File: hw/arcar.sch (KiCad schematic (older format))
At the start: 55 parts, among them J1 USB_B_Micro, J2 GPIO, J3 MOTOR, M1 screw, M2 screw, M3 screw, P1 AVR_ISP_02X03, SW1 SW_Push, U1 USBLC6-2SC6, U2 ATMEGA328PB-AU, U3 CP2102, U4 ULN2003A, U5 LSM9DS1, U6 ULN2003A, U7 TLE52062GAUMA1, U8 RN4871

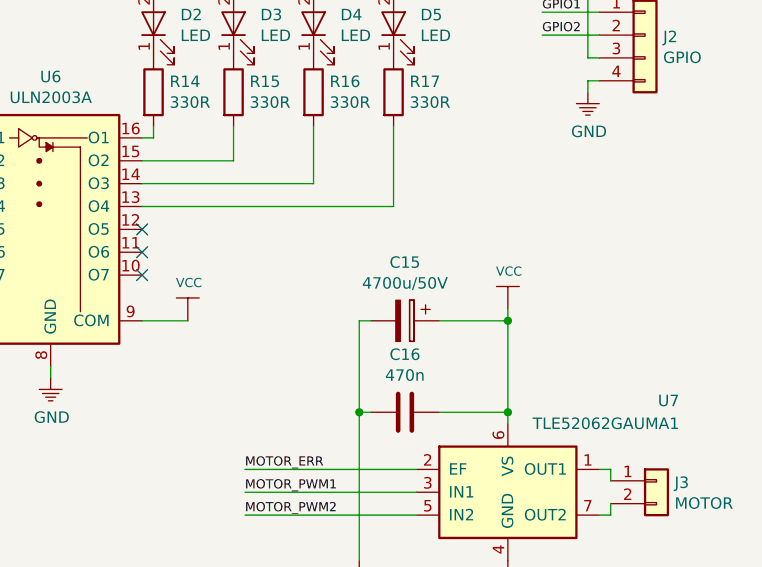
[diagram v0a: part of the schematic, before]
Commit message: assigned footprints
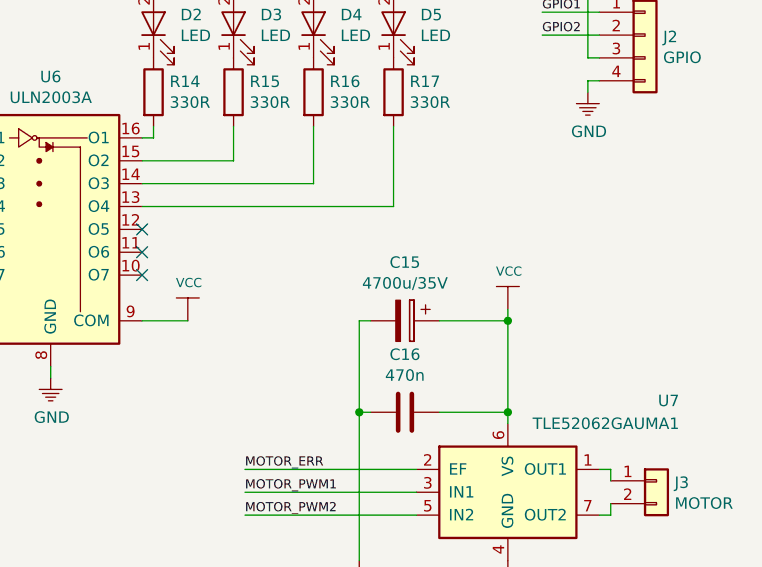
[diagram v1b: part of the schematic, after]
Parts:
- C1, C10, C11, C12, C13, C14, C16, C2, C3, C4, C5, C6, C7, C8, C9: footprint (none) -> Capacitors_SMD:C_0805_HandSoldering
- C15: value 4700u/50V -> 4700u/35V; footprint (none) -> Capacitors_THT:CP_Radial_D18.0mm_P7.50mm
- D1: footprint (none) -> Diodes_SMD:D_SMA
- D2, D3, D4, D5: footprint (none) -> LEDs:LED_D3.0mm_FlatTop
- J1: footprint Connectors:USB_Micro-B_10103594-0001LF -> Connectors_USB:USB_Micro-B_Wuerth-614105150721_Vertical_CircularHoles
- J2: footprint (none) -> Pin_Headers:Pin_Header_Straight_1x04_Pitch2.54mm
- J3: footprint (none) -> Pin_Headers:Pin_Header_Straight_1x02_Pitch2.54mm
- M1, M2, M3: footprint (none) -> wyk_mech:screw_M3
- R1, R10, R11, R12, R13, R14, R15, R16, R17, R2, R3, R4, R5, R6, R7, R8, R9: footprint (none) -> Resistors_SMD:R_0805_HandSoldering
- SW1: footprint (none) -> Buttons_Switches_THT:SW_PUSH_6mm_h5mm
- U4, U6: footprint (none) -> Housings_SOIC:SOIC-16_3.9x9.9mm_Pitch1.27mm
- U8: footprint (none) -> wyk_rf_modules:RN4871

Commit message: assigned footprints
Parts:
- AFF1: footprint Displays_7-Segment:LTS-69xx -> Displays_7-Segment:7SegmentLED_LTS6760_LTS6780
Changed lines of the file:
@@
 F 0 "AFF1" H 6750 2267 50  0000 C CNN
 F 1 "LTS-6960HR" H 6750 2176 50  0000 C CNN
-F 2 "Displays_7-Segment:LTS-69xx" H 6750 1100 50  0001 C CNN
+F 2 "Displays_7-Segment:7SegmentLED_LTS6760_LTS6780" H 6750 1100 50  0001 C CNN
 F 3 "Display/LTC-6960HR.pdf" H 6750 1600 50  0001 C CNN
 	1    6750 1600

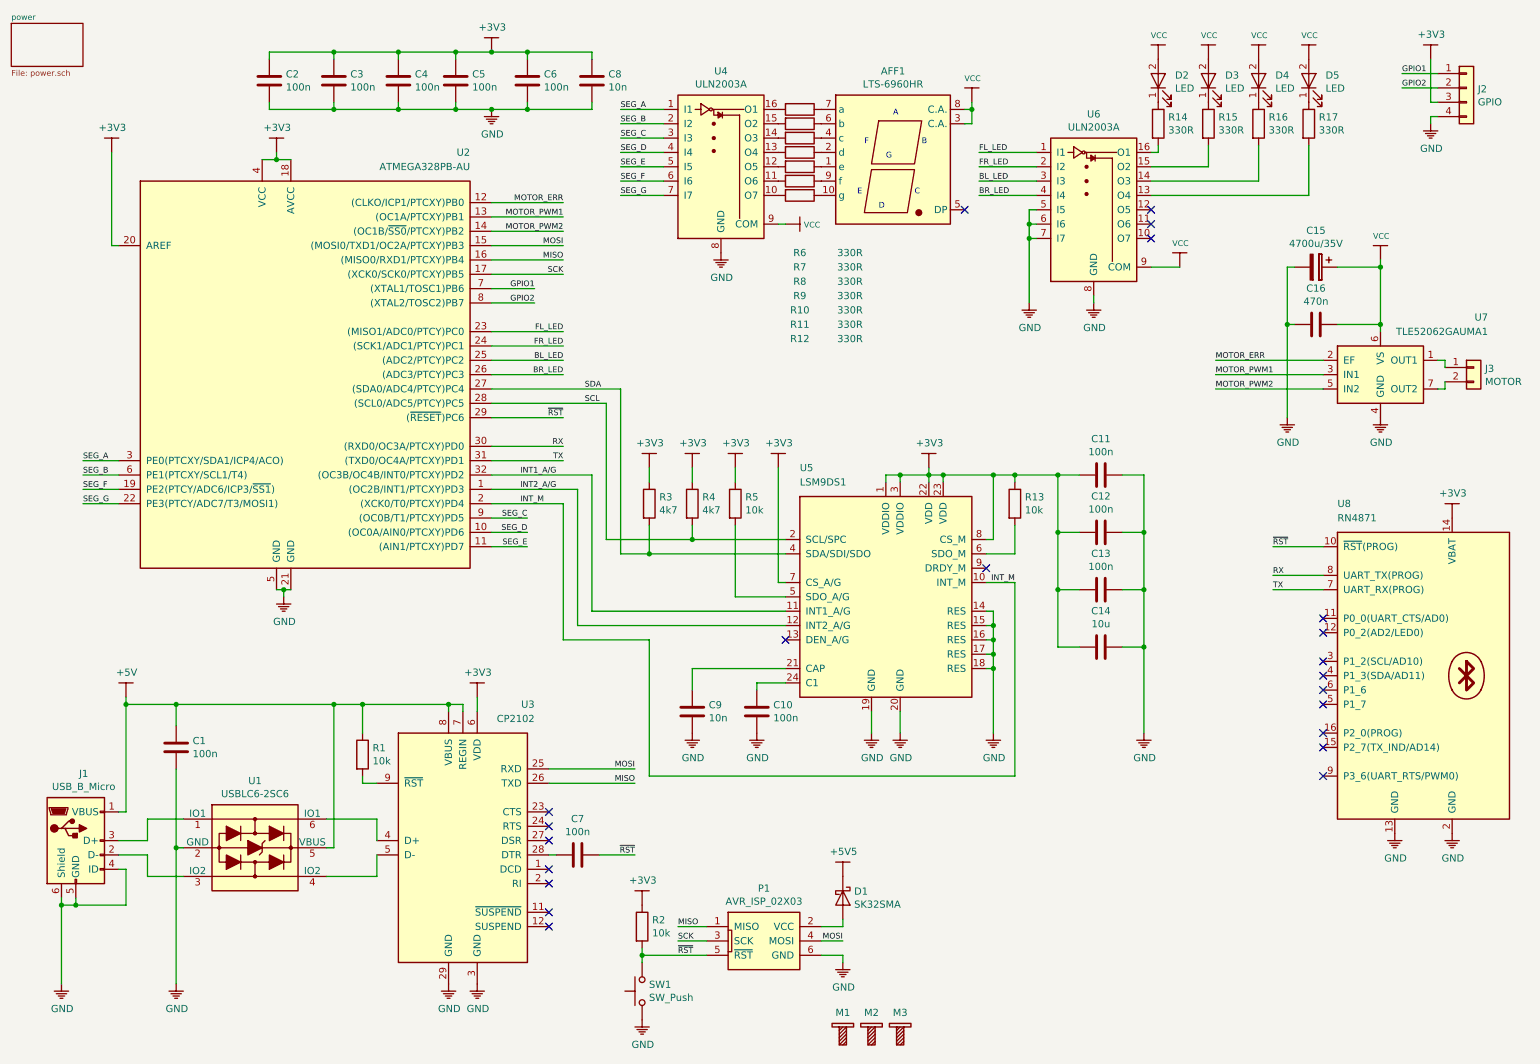
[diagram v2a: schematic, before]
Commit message: reduced schematic
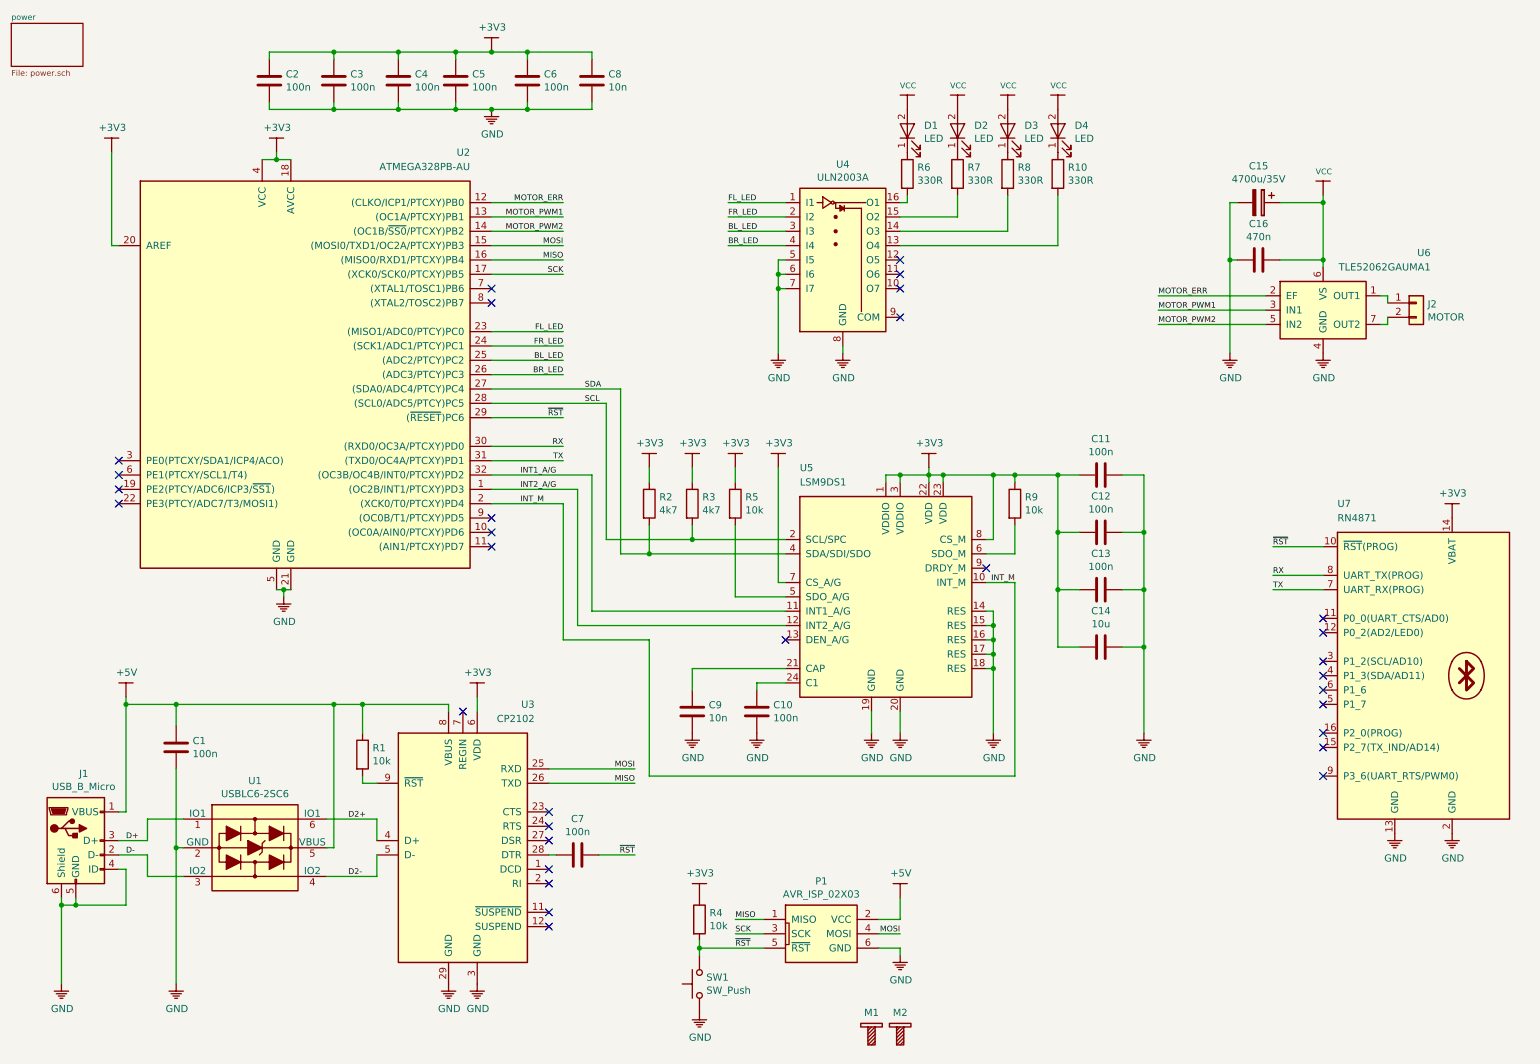
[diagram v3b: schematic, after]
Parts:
- removed AFF1: LTS-6960HR, Displays_7-Segment:7SegmentLED_LTS6760_LTS6780, symbol LTS-6960HR
- removed D1: SK32SMA, Diodes_SMD:D_SMA, symbol D_Schottky
- removed J2: GPIO, Pin_Headers:Pin_Header_Straight_1x04_Pitch2.54mm, symbol Conn_01x04
- removed M3: screw, wyk_mech:screw_M3, symbol screw
- removed R10, R11, R12, R6, R7, R8, R9: 330R, Resistors_SMD:R_0805_HandSoldering, symbol R
- removed U4: ULN2003A, Housings_SOIC:SOIC-16_3.9x9.9mm_Pitch1.27mm, symbol ULN2003A
- C15: footprint Capacitors_THT:CP_Radial_D18.0mm_P7.50mm -> Capacitors_THT:CP_Radial_D4.0mm_P1.50mm
- renumbered D2 to D1, D3 to D2, D4 to D3, D5 to D4, J3 to J2, R17 to R10, R3 to R2, R4 to R3, R2 to R4, R14 to R6, R15 to R7, R16 to R8, R13 to R9, U6 to U4, U7 to U6, U8 to U7
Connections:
- net +5V: now also P1.2 (VCC); no longer U3.7 (REGIN)
- net VCC: no longer U4.9 (COM)
- net D-: now reaches J1.2 (D-), U1.3 (IO2)
- net D+: now reaches J1.3 (D+), U1.1 (IO1)
- net D2-: now reaches U1.4 (IO2), U3.5 (D-)
- net D2+: now reaches U1.6 (IO1), U3.4 (D+)
- net GPIO1: no longer names the net of U2.7 ((XTAL1/TOSC1)PB6)
- net GPIO2: no longer names the net of U2.8 ((XTAL2/TOSC2)PB7)
- net SEG_A: no longer names the net of U2.3 (PE0(PTCXY/SDA1/ICP4/ACO))
- net SEG_B: no longer names the net of U2.6 (PE1(PTCXY/SCL1/T4))
- net SEG_C: no longer names the net of U2.9 ((OC0B/T1/PTCXY)PD5)
- net SEG_D: no longer names the net of U2.10 ((OC0A/AIN0/PTCXY)PD6)
- net SEG_E: no longer names the net of U2.11 ((AIN1/PTCXY)PD7)
- net SEG_F: no longer names the net of U2.19 (PE2(PTCY/ADC6/ICP3/~SS1~))
- net SEG_G: no longer names the net of U2.22 (PE3(PTCY/ADC7/T3/MOSI1))
- no-connect marks 22 -> 32
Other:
- note removed: "A"
- note removed: "B"
- note removed: "C"
- note removed: "D"
- note removed: "E"
- note removed: "F"
- note removed: "G"
- moved on the sheet: C15, C16, D1, D2, D3, D4, J2, M1, M2, P1, R10, R4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

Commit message: big reduced change all power source
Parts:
- added C17: 4700u/35V, Capacitors_THT:CP_Radial_D4.0mm_P1.50mm, symbol CP
- added C18, C19: 1u/50V, Capacitors_SMD:C_0805_HandSoldering, symbol C
- added D5, D6, D7, D8, D9: SK32SMA, Diodes_SMD:D_SMA, symbol D_Schottky
- added J3: POWER, Pin_Headers:Pin_Header_Straight_1x02_Pitch2.54mm, symbol Conn_01x02
- added U8: MCP1804T-3302I/DB, TO_SOT_Packages_SMD:SOT-223, symbol MCP1804T-3302I/DB
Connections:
- net +5V is gone; now on net VCC: C1.1, J1.1 (VBUS), P1.2 (VCC), R1.1, U1.5 (VBUS), U3.8 (VBUS)
- net +3V3: now also C19.1, U8.3 (VO)
- net GND: now also C17.2, C18.2, C19.2, D6.2 (A), D8.2 (A), U8.2 (GND)
- net VCC: now also D5.1 (K), D7.1 (K), D9.2 (A)
- new net: D7.2 (A), D8.1 (K), J3.1 (Pin_1)
- new net: D5.2 (A), D6.1 (K), J3.2 (Pin_2)
- new net: C17.1, C18.1, D9.1 (K), U8.1 (VI)
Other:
- moved on the sheet: C15, C16, C2, C3, C4, C5, C6, C8, D1, D2, D3, D4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

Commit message: all the components are placed on the board
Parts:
- D1, D2, D3, D4: footprint LEDs:LED_D3.0mm_FlatTop -> Pin_Headers:Pin_Header_Straight_1x02_Pitch2.54mm
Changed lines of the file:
@@
 F 0 "D1" V 5988 1083 50  0000 R CNN
 F 1 "LED" V 5897 1083 50  0000 R CNN
-F 2 "LEDs:LED_D3.0mm_FlatTop" H 5950 1200 50  0001 C CNN
+F 2 "Pin_Headers:Pin_Header_Straight_1x02_Pitch2.54mm" H 5950 1200 50  0001 C CNN
 F 3 "" H 5950 1200 50  0001 C CNN
 	1    5950 1200
@@
 F 0 "D2" V 6338 1083 50  0000 R CNN
 F 1 "LED" V 6247 1083 50  0000 R CNN
-F 2 "LEDs:LED_D3.0mm_FlatTop" H 6300 1200 50  0001 C CNN
+F 2 "Pin_Headers:Pin_Header_Straight_1x02_Pitch2.54mm" H 6300 1200 50  0001 C CNN
 F 3 "" H 6300 1200 50  0001 C CNN
 	1    6300 1200
@@
 F 0 "D3" V 6688 1083 50  0000 R CNN
 F 1 "LED" V 6597 1083 50  0000 R CNN
-F 2 "LEDs:LED_D3.0mm_FlatTop" H 6650 1200 50  0001 C CNN
+F 2 "Pin_Headers:Pin_Header_Straight_1x02_Pitch2.54mm" H 6650 1200 50  0001 C CNN
 F 3 "" H 6650 1200 50  0001 C CNN
 	1    6650 1200
@@
 F 0 "D4" V 7038 1083 50  0000 R CNN
 F 1 "LED" V 6947 1083 50  0000 R CNN
-F 2 "LEDs:LED_D3.0mm_FlatTop" H 7000 1200 50  0001 C CNN
+F 2 "Pin_Headers:Pin_Header_Straight_1x02_Pitch2.54mm" H 7000 1200 50  0001 C CNN
 F 3 "" H 7000 1200 50  0001 C CNN
 	1    7000 1200
@@
 	5950 1700 5950 1650
 Wire Wire Line
-	5400 7000 5400 7050
-Wire Wire Line
-	5400 7050 5400 7100
+	5400 7000 5400 7100
 Connection ~ 5400 7050
 Wire Wire Line
@@
 	9750 4250 9400 4250
 Wire Wire Line
-	2450 4550 2500 4550
-Wire Wire Line
-	2500 4550 2550 4550
+	2450 4550 2550 4550
 Wire Wire Line
 	2500 4600 2500 4550
 Connection ~ 2500 4550
 Wire Wire Line
-	2350 1550 2450 1550
-Wire Wire Line
-	2450 1550 2550 1550
+	2350 1550 2550 1550
 Wire Wire Line
 	2450 1500 2450 1550
@@
 	2850 6350 2850 5350
 Wire Wire Line
-	1750 5800 1750 6350
-Wire Wire Line
-	1750 6350 1750 7300
+	1750 5800 1750 7300
 Wire Wire Line
 	1750 6350 1800 6350
@@
 	1400 6100 1350 6100
 Wire Wire Line
-	1400 5300 1400 5350
-Wire Wire Line
-	1400 5350 1400 6100
+	1400 5300 1400 6100
 Wire Wire Line
 	1350 6500 1400 6500
@@
 	9700 3400 8950 3400
 Wire Wire Line
-	5050 2100 5050 2200
-Wire Wire Line
-	5050 2200 5050 2300
-Wire Wire Line
-	5050 2300 5050 2700
+	5050 2100 5050 2700
 Wire Wire Line
 	5050 2100 5100 2100
@@
 Connection ~ 5050 2300
 Wire Wire Line
-	10100 2500 10100 2550
-Wire Wire Line
-	10100 2550 10100 2950
-Wire Wire Line
-	10100 2950 10100 3000
+	10100 2500 10100 3000
 Wire Wire Line
 	9800 2950 10100 2950
@@
 Connection ~ 10100 2550
 Wire Wire Line
-	9450 2550 9450 2950
-Wire Wire Line
-	9450 2950 9450 3600
+	9450 2550 9450 3600
 Wire Wire Line
 	9450 2550 9500 2550
@@
 	7250 2700 7250 2750
 Wire Wire Line
-	6350 2700 6800 2700
-Wire Wire Line
-	6800 2700 7250 2700
-Wire Wire Line
-	7250 2700 7650 2700
-Wire Wire Line
-	7650 2700 7900 2700
-Wire Wire Line
-	7900 2700 8150 2700
-Wire Wire Line
-	8150 2700 8600 2700
+	6350 2700 8600 2700
 Wire Wire Line
 	8600 2700 8600 2750
@@
 	7250 3100 7250 3050
 Wire Wire Line
-	6350 3100 6800 3100
-Wire Wire Line
-	6800 3100 7250 3100
-Wire Wire Line
-	7250 3100 7650 3100
-Wire Wire Line
-	7650 3100 7900 3100
-Wire Wire Line
-	7900 3100 8150 3100
-Wire Wire Line
-	8150 3100 8600 3100
+	6350 3100 8600 3100
 Wire Wire Line
 	8600 3100 8600 3050
@@
 	3950 3950 4450 3950
 Wire Wire Line
-	7000 3700 7000 3750
-Wire Wire Line
-	7000 3750 7000 3800
+	7000 3700 7000 3800
 Wire Wire Line
 	7100 3750 7100 3800
 Wire Wire Line
-	6700 3750 6800 3750
-Wire Wire Line
-	6800 3750 7000 3750
-Wire Wire Line
-	7000 3750 7100 3750
-Wire Wire Line
-	7100 3750 7450 3750
-Wire Wire Line
-	7450 3750 7600 3750
-Wire Wire Line
-	7600 3750 7900 3750
-Wire Wire Line
-	7900 3750 8050 3750
+	6700 3750 8050 3750
 Connection ~ 7000 3750
 Wire Wire Line
@@
 Connection ~ 6800 3750
 Wire Wire Line
-	7450 4700 7450 4800
-Wire Wire Line
-	7450 4800 7450 4900
-Wire Wire Line
-	7450 4900 7450 5000
-Wire Wire Line
-	7450 5000 7450 5100
-Wire Wire Line
-	7450 5100 7450 5550
+	7450 4700 7450 5550
 Wire Wire Line
 	7450 4700 7400 4700
@@
 Connection ~ 7100 3750
 Wire Wire Line
-	4750 4200 5350 4200
-Wire Wire Line
-	5350 4200 6000 4200
+	4750 4200 6000 4200
 Wire Wire Line
 	5350 4100 5350 4200
@@
 	4850 3150 4850 4300
 Wire Wire Line
-	4850 4300 5050 4300
-Wire Wire Line
-	5050 4300 6000 4300
+	4850 4300 6000 4300
 Wire Wire Line
 	3950 3250 4750 3250
@@
 	4750 3250 4750 4200
 Wire Wire Line
-	8500 3750 8500 4150
-Wire Wire Line
-	8500 4150 8500 4550
-Wire Wire Line
-	8500 4550 8500 4950
-Wire Wire Line
-	8500 4950 8500 5550
+	8500 3750 8500 5550
 Wire Wire Line
 	8500 3750 8350 3750
 Wire Wire Line
-	7900 3750 7900 4150
-Wire Wire Line
-	7900 4150 7900 4550
-Wire Wire Line
-	7900 4550 7900 4950
+	7900 3750 7900 4950
 Wire Wire Line
 	7900 4950 8050 4950
@@
 	1050 6750 1050 6700
 Wire Wire Line
-	950  6750 1050 6750
-Wire Wire Line
-	1050 6750 1400 6750
-Wire Wire Line
-	950  6700 950  6750
-Wire Wire Line
-	950  6750 950  7300
+	950  6750 1400 6750
+Wire Wire Line
+	950  6700 950  7300
 Wire Wire Line
 	1400 6750 1400 6500
@@
 $EndComp
 Wire Wire Line
-	1400 5350 1750 5350
-Wire Wire Line
-	1750 5350 2850 5350
-Wire Wire Line
-	2850 5350 3050 5350
-Wire Wire Line
-	3050 5350 3650 5350
+	1400 5350 3650 5350
 NoConn ~ 3750 5400
 Wire Wire Line
@@
 $EndComp
 Wire Wire Line
-	8950 1050 8950 1100
-Wire Wire Line
-	8950 1100 8950 1400
+	8950 1050 8950 1400
 Connection ~ 8950 1100
 $Comp
@@
 $EndComp
 Wire Wire Line
-	7950 1100 8300 1100
-Wire Wire Line
-	8300 1100 8550 1100
+	7950 1100 8550 1100
 $Comp
 L GND #PWR040
@@
 $EndComp
 Wire Wire Line
-	7950 1050 7950 1100
-Wire Wire Line
-	7950 1100 7950 1150
-Wire Wire Line
-	8300 1050 8300 1100
-Wire Wire Line
-	8300 1100 8300 1150
+	7950 1050 7950 1150
+Wire Wire Line
+	8300 1050 8300 1150
 Connection ~ 8300 1100
 Wire Wire Line
 	7800 1500 7950 1500
 Wire Wire Line
-	7950 1450 7950 1500
-Wire Wire Line
-	7950 1500 7950 1650
+	7950 1450 7950 1650
 Wire Wire Line
 	7800 1600 8300 1600
 Wire Wire Line
-	8300 1450 8300 1600
-Wire Wire Line
-	8300 1600 8300 1650
+	8300 1450 8300 1650
 Connection ~ 7950 1500
 Connection ~ 8300 1600
@@
 	10150 1950 10150 1400
 Wire Wire Line
-	8850 1100 8950 1100
-Wire Wire Line
-	8950 1100 9650 1100
-Wire Wire Line
-	9650 1100 9850 1100
+	8850 1100 9850 1100
 Wire Wire Line
 	9650 1400 9650 1100
 Connection ~ 9650 1100
 Wire Wire Line
-	10650 1050 10650 1100
-Wire Wire Line
-	10650 1100 10650 1400
+	10650 1050 10650 1400
 Wire Wire Line
 	10650 1100 10450 1100

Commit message: all routed
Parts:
- U8: footprint TO_SOT_Packages_SMD:SOT-223 -> TO_SOT_Packages_SMD:SOT-223-3_TabPin2
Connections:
- net MOTOR_PWM1: now also U2.14 ((OC1B/~SS0~/PTCXY)PB2); no longer U2.13 ((OC1A/PTCXY)PB1)
- net MOTOR_PWM2: now also U2.13 ((OC1A/PTCXY)PB1); no longer U2.14 ((OC1B/~SS0~/PTCXY)PB2)
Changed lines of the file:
@@
 	1    0    0    -1
 $EndComp
+Text Label 4450 2050 2    40   ~ 0
+MOTOR_PWM1
 Text Label 4450 1950 2    40   ~ 0
-MOTOR_PWM1
-Text Label 4450 2050 2    40   ~ 0
 MOTOR_PWM2
 $Comp
@@
 Connection ~ 7950 1100
 $Comp
-L MCP1804T-3302I/DB U8
-U 1 1 5A013302
-P 10150 1100
-F 0 "U8" H 10150 1342 50  0000 C CNN
-F 1 "MCP1804T-3302I/DB" H 10150 1251 50  0000 C CNN
-F 2 "TO_SOT_Packages_SMD:SOT-223" H 10150 1450 50  0001 C CNN
-F 3 "http://ww1.microchip.com/downloads/en/DeviceDoc/20002200D.pdf" H 10150 1350 50  0001 C CNN
-	1    10150 1100
-	1    0    0    -1
-$EndComp
-$Comp
 L C C18
 U 1 1 5A013309
@@
 	1    0    0    -1
 $EndComp
+$Comp
+L MCP1804T-3302I/DB U8
+U 1 1 5A013254
+P 10150 1100
+F 0 "U8" H 10150 1342 50  0000 C CNN
+F 1 "MCP1804T-3302I/DB" H 10150 1251 50  0000 C CNN
+F 2 "TO_SOT_Packages_SMD:SOT-223-3_TabPin2" H 10150 1450 50  0001 C CNN
+F 3 "http://ww1.microchip.com/downloads/en/DeviceDoc/20002200D.pdf" H 10150 1350 50  0001 C CNN
+	1    10150 1100
+	1    0    0    -1
+$EndComp
